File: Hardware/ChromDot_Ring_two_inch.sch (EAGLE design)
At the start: 25 parts, among them J1 DOUBLE_LED_PAD, J2 DOUBLE_LED_PAD, J3 DOUBLE_LED_PAD, J4 DOUBLE_LED_PAD

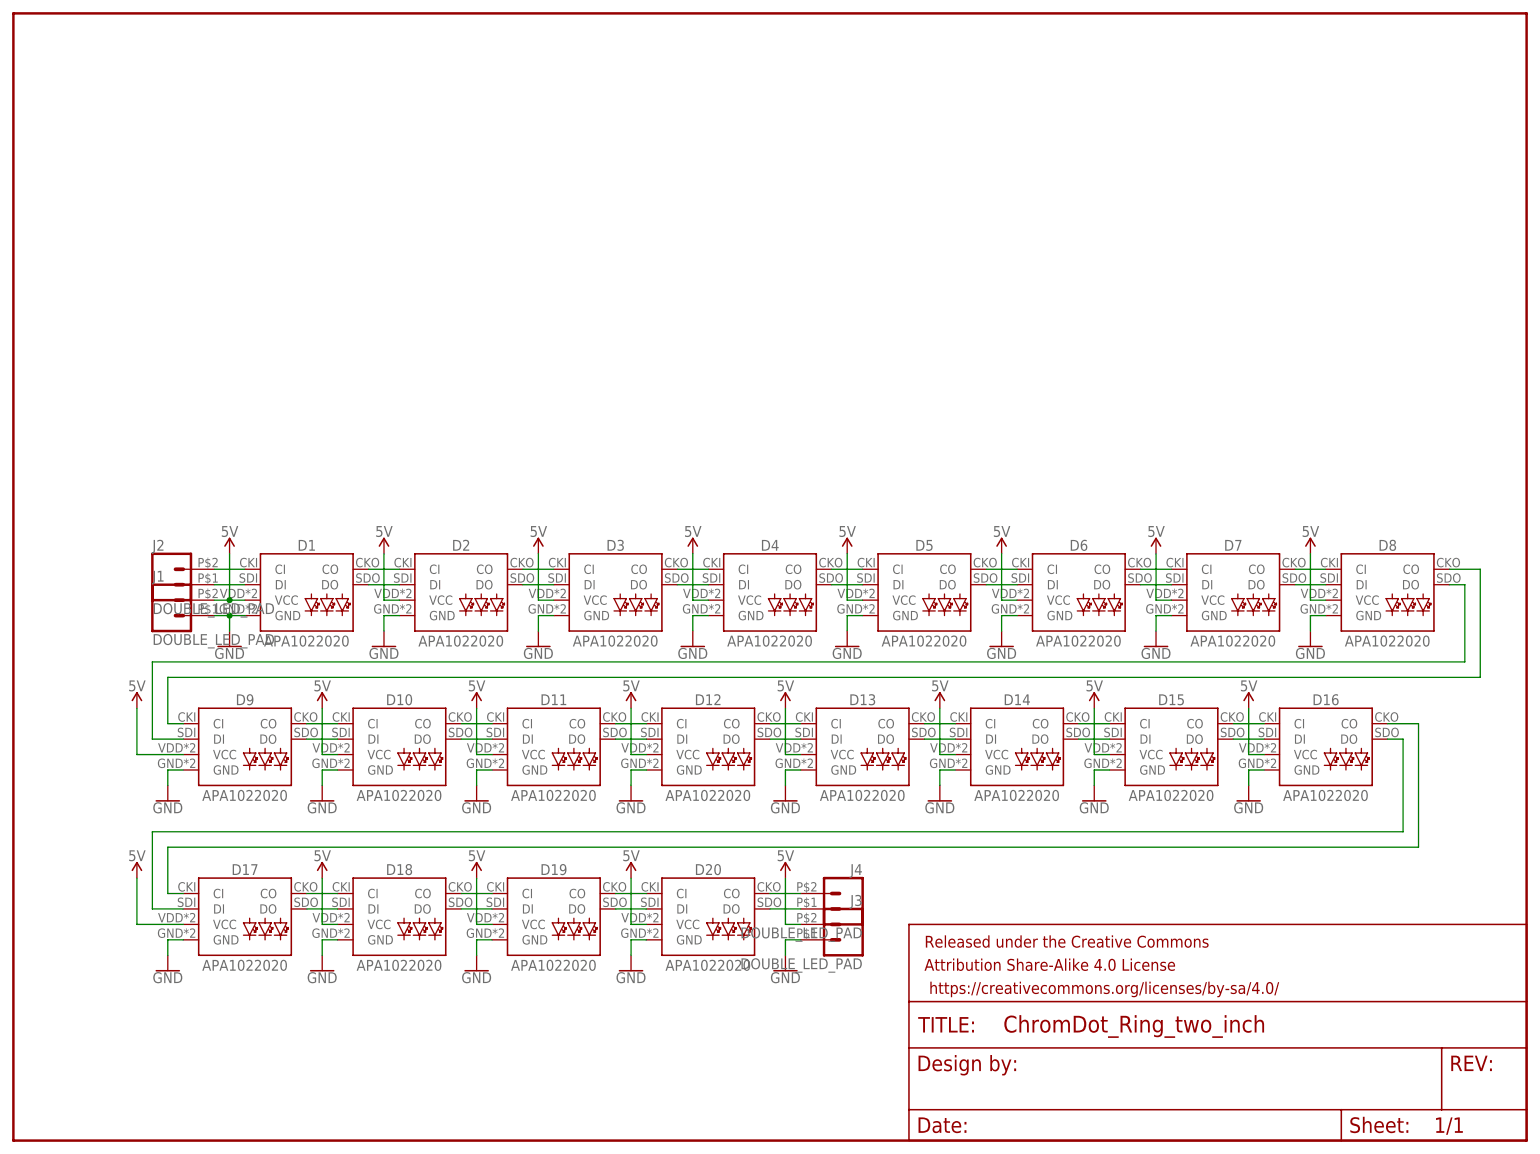
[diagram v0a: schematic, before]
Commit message: adding apa102 rings
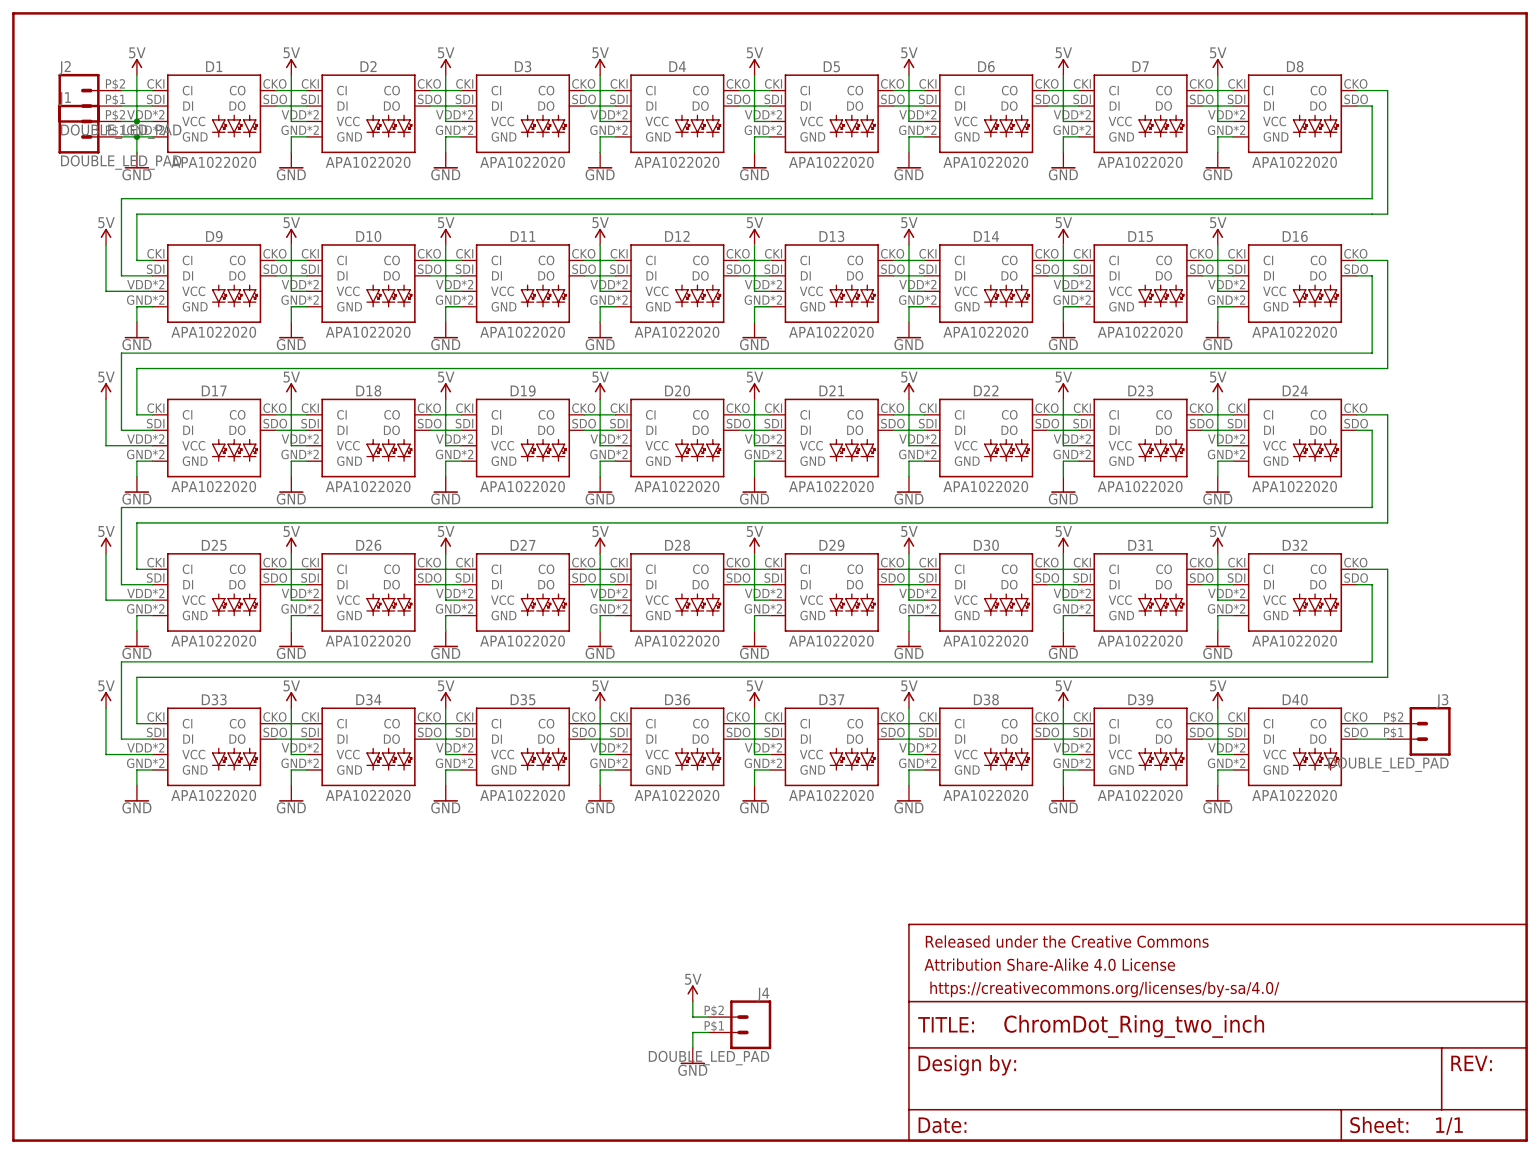
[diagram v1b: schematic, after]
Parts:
- added D21, D22, D23, D24, D25, D26, D27, D28, D29, D30, D31, D32, D33, D34, D35, D36, D37, D38, D39, D40: APA1022020, SparkFun-LED:APA1022020
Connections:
- new net N$133: D40.CO, J3.2
- new net N$134: D40.DO, J3.1
- new net N$17: D24.CO, D25.CI
- new net N$47: D24.DO, D25.DI
- new net N$48: D21.CO, D22.CI
- new net N$49: D21.DO, D22.DI
- new net N$50: D22.CO, D23.CI
- new net N$51: D22.DO, D23.DI
- new net N$52: D23.CO, D24.CI
- new net N$53: D23.DO, D24.DI
- new net N$54: D32.DO, D33.DI
- new net N$55: D32.CO, D33.CI
- new net N$56: D25.CO, D26.CI
- new net N$57: D25.DO, D26.DI
- new net N$58: D26.CO, D27.CI
- new net N$59: D26.DO, D27.DI
- new net N$60: D27.CO, D28.CI
- new net N$61: D27.DO, D28.DI
- new net N$62: D28.CO, D29.CI
- new net N$63: D28.DO, D29.DI
- new net N$66: D29.CO, D30.CI
- new net N$67: D29.DO, D30.DI
- new net N$68: D30.CO, D31.CI
- new net N$69: D30.DO, D31.DI
- new net N$70: D31.CO, D32.CI
- new net N$71: D31.DO, D32.DI
- new net N$74: D33.CO, D34.CI
- new net N$75: D33.DO, D34.DI
- new net N$76: D34.CO, D35.CI
- new net N$77: D34.DO, D35.DI
- new net N$78: D35.CO, D36.CI
- new net N$79: D35.DO, D36.DI
- new net N$80: D36.CO, D37.CI
- new net N$81: D36.DO, D37.DI
- new net N$84: D37.CO, D38.CI
- new net N$85: D37.DO, D38.DI
- new net N$86: D38.CO, D39.CI
- new net N$87: D38.DO, D39.DI
- new net N$88: D39.CO, D40.CI
- new net N$89: D39.DO, D40.DI
- net 5V: now also D21.VCC, D22.VCC, D23.VCC, D24.VCC, D25.VCC, D26.VCC, D27.VCC, D28.VCC, D29.VCC, D30.VCC, D31.VCC, D32.VCC, D33.VCC, D34.VCC, D35.VCC, D36.VCC, D37.VCC, D38.VCC, D39.VCC, D40.VCC, J4.2; no longer J3.2
- net GND: now also D21.GND, D22.GND, D23.GND, D24.GND, D25.GND, D26.GND, D27.GND, D28.GND, D29.GND, D30.GND, D31.GND, D32.GND, D33.GND, D34.GND, D35.GND, D36.GND, D37.GND, D38.GND, D39.GND, D40.GND, J4.1; no longer J3.1
- net N$41: now also D21.CI; no longer J4.2
- net N$42: now also D21.DI; no longer J4.1
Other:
- moved on the sheet: D1, D10, D11, D12, D13, D14, D15, D16, D17, D18, D19, D2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
